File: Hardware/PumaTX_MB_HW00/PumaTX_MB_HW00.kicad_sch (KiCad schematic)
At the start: 107 parts, among them J100 FH12A-26S-0.5SH_55_, J101 FH12-12S-0.5SH_55_, J102 500334-0160, J103 500334-0160, J104 692122030100, J105 53398-0667, J300 U.FL-R-SMT-1_40_, J410 U.FL-R-SMT-1_40_, M130 Motor_DC, M140 Fan, Q130 ZXMN3B01F, Q140 ZXMN3B01F, Q200 UMH3NTN, Q201 UMH3NTN, U200 CP2105-F01-GMR, U300 ESP32-PICO-D4, U400 ESP32-PICO-D4, U402 E28-2G4M27S, U410 SX1280, U500 BQ24075RGTR, U510 MIC5528-3.3YMT-T5, U520 MIC5528-3.3YMT-T5, U530 MIC5528-3.3YMT-T5, Y410 NX2016SA-52MHZ-EXS00A-CS06016

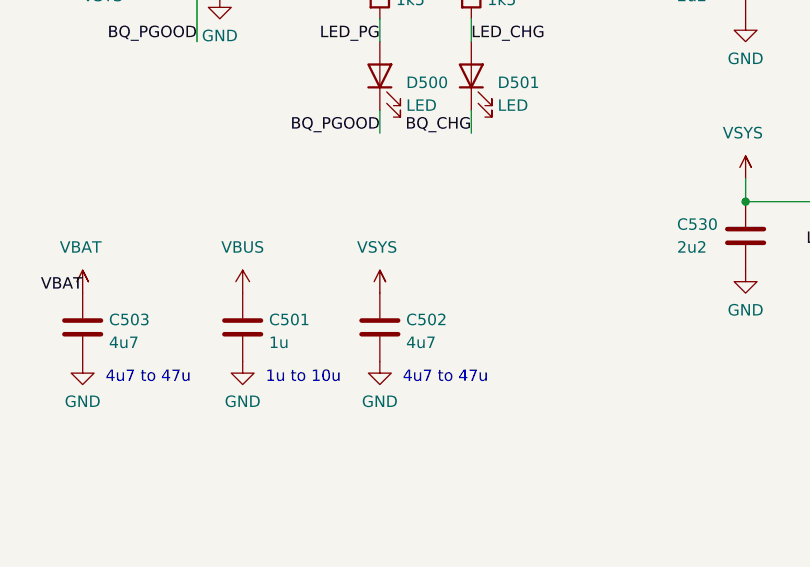
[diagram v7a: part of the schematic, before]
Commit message: Started layout
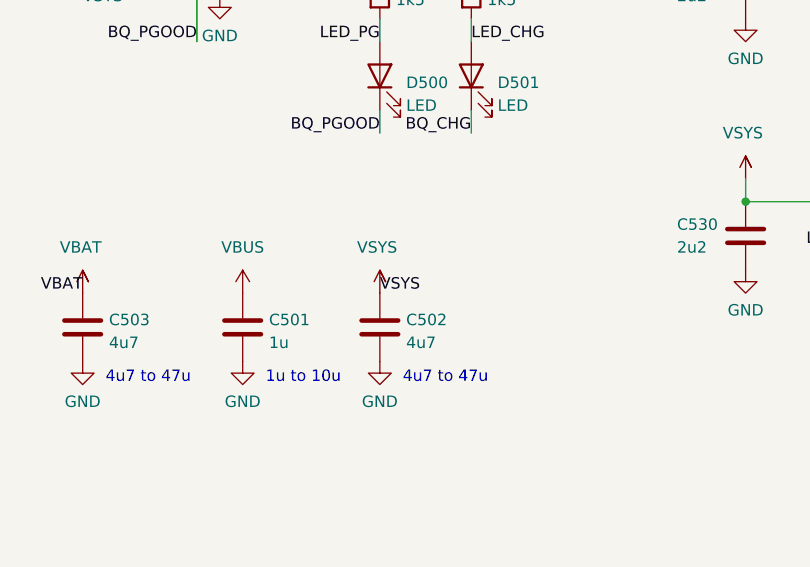
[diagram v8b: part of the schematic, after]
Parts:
- D200: Mouser Price/Stock https://www.mouser.co.uk/ProductDetail/Littelfuse/SP0503BAH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 -> https://www.mouser.fr/datasheet/2/240/Littelfuse_TVS_Diode_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
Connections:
- net VSYS: now also C502.1
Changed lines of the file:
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@@
     (effects (font (size 1.27 1.27)) (justify left bottom))
   )
+  (label "VSYS" (at 444.5 307.34 0)
+    (effects (font (size 1.27 1.27)) (justify left bottom))
+  )
   (label "ELRS_DTR" (at 447.04 73.66 0)
     (effects (font (size 1.27 1.27)) (justify left bottom))
@@
     (pin "1")
   )
-  (symbol (lib_id "Component lib:SP0503BAHTG") (at 548.64 86.36 90) (unit 1)
-    (in_bom yes) (on_board yes)
-    (property "Reference" "D200" (id 0) (at 553.847 80.4199 90)
-      (effects (font (size 1.27 1.27)) (justify right))
-    )
-    (property "Value" "SP0503BAHTG" (id 1) (at 553.847 82.9568 90)
-      (effects (font (size 1.27 1.27)) (justify right))
-    )
-    (property "Footprint" "Component_lib:SP0503BAHTG" (id 2) (at 541.02 63.5 0)
-      (effects (font (size 1.27 1.27)) (justify left) hide)
-    )
-    (property "Datasheet" "" (id 3) (at 541.02 62.23 0)
-      (effects (font (size 1.27 1.27)) (justify left) hide)
-    )
-    (property "Description" "ESD Suppressors / TVS Diodes TVS AVAL DIODE SMT" (id 4) (at 543.56 63.5 0)
-      (effects (font (size 1.27 1.27)) (justify left) hide)
-    )
-    (property "Height" "1.22" (id 5) (at 546.1 63.5 0)
-      (effects (font (size 1.27 1.27)) (justify left) hide)
-    )
-    (property "Mouser Part Number" "576-SP0503BAHTG" (id 6) (at 548.64 63.5 0)
-      (effects (font (size 1.27 1.27)) (justify left) hide)
-    )
-    (property "Mouser Price/Stock" "https://www.mouser.co.uk/ProductDetail/Littelfuse/SP0503BAHTG?qs=uD%2FdkN7XIa0NTYXwHdELYA%3D%3D" (id 7) (at 551.18 63.5 0)
-      (effects (font (size 1.27 1.27)) (justify left) hide)
-    )
-    (property "Manufacturer_Name" "LITTELFUSE" (id 8) (at 553.72 63.5 0)
-      (effects (font (size 1.27 1.27)) (justify left) hide)
-    )
-    (property "Manufacturer_Part_Number" "SP0503BAHTG" (id 9) (at 556.26 63.5 0)
-      (effects (font (size 1.27 1.27)) (justify left) hide)
-    )
-    (pin "1")
-    (pin "2")
-    (pin "3")
-    (pin "4")
-  )
   (symbol (lib_id "Component_lib:L") (at 48.26 233.68 0) (unit 1)
     (in_bom yes) (on_board yes) (fields_autoplaced)
@@
     (pin "1")
   )
+  (symbol (lib_name "SP0503BAHTG_1") (lib_id "Component lib:SP0503BAHTG") (at 548.64 86.36 90) (unit 1)
+    (in_bom yes) (on_board yes) (fields_autoplaced)
+    (property "Reference" "D200" (id 0) (at 553.847 80.4199 90)
+      (effects (font (size 1.27 1.27)) (justify right))
+    )
+    (property "Value" "SP0503BAHTG" (id 1) (at 553.847 82.9568 90)
+      (effects (font (size 1.27 1.27)) (justify right))
+    )
+    (property "Footprint" "Component_lib:SP0503BAHTG" (id 2) (at 541.02 63.5 0)
+      (effects (font (size 1.27 1.27)) (justify left) hide)
+    )
+    (property "Datasheet" "https://www.mouser.fr/datasheet/2/240/Littelfuse_TVS_Diode_Array_SP05_Datasheet_pdf-777043.pdf" (id 3) (at 558.8 63.5 0)
+      (effects (font (size 1.27 1.27)) (justify left) hide)
+    )
+    (property "Description" "ESD Suppressors / TVS Diodes TVS AVAL DIODE SMT" (id 4) (at 543.56 63.5 0)
+      (effects (font (size 1.27 1.27)) (justify left) hide)
+    )
+    (property "Height" "1.22" (id 5) (at 546.1 63.5 0)
+      (effects (font (size 1.27 1.27)) (justify left) hide)
+    )
+    (property "Mouser Part Number" "576-SP0503BAHTG" (id 6) (at 548.64 63.5 0)
+      (effects (font (size 1.27 1.27)) (justify left) hide)
+    )
+    (property "Mouser Price/Stock" "https://www.mouser.fr/datasheet/2/240/Littelfuse_TVS_Diode_Array_SP05_Datasheet_pdf-777043.pdf" (id 7) (at 551.18 63.5 0)
+      (effects (font (size 1.27 1.27)) (justify left) hide)
+    )
+    (property "Manufacturer_Name" "LITTELFUSE" (id 8) (at 553.72 63.5 0)
+      (effects (font (size 1.27 1.27)) (justify left) hide)
+    )
+    (property "Manufacturer_Part_Number" "SP0503BAHTG" (id 9) (at 556.26 63.5 0)
+      (effects (font (size 1.27 1.27)) (justify left) hide)
+    )
+    (pin "1")
+    (pin "2")
+    (pin "3")
+    (pin "4")
+  )
   (symbol (lib_id "Component_lib:ZXMN3B01F") (at 215.9 144.78 0) (unit 1)
     (in_bom yes) (on_board yes) (fields_autoplaced)
@@
       (reference "D140") (unit 1) (value "S1GHE") (footprint "Component_lib:S1GHE")
     )
-    (path "/8fcd37e0-ed5c-4179-a5f5-fa54d38866d1"
+    (path "/b822a2dc-7dba-4a87-99c7-a460a312b37c"
       (reference "D200") (unit 1) (value "SP0503BAHTG") (footprint "Component_lib:SP0503BAHTG")
     )
